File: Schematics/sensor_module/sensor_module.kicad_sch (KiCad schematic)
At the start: 4 parts, among them J1 HAL_SENS, J2 PT_1, J3 PT_2

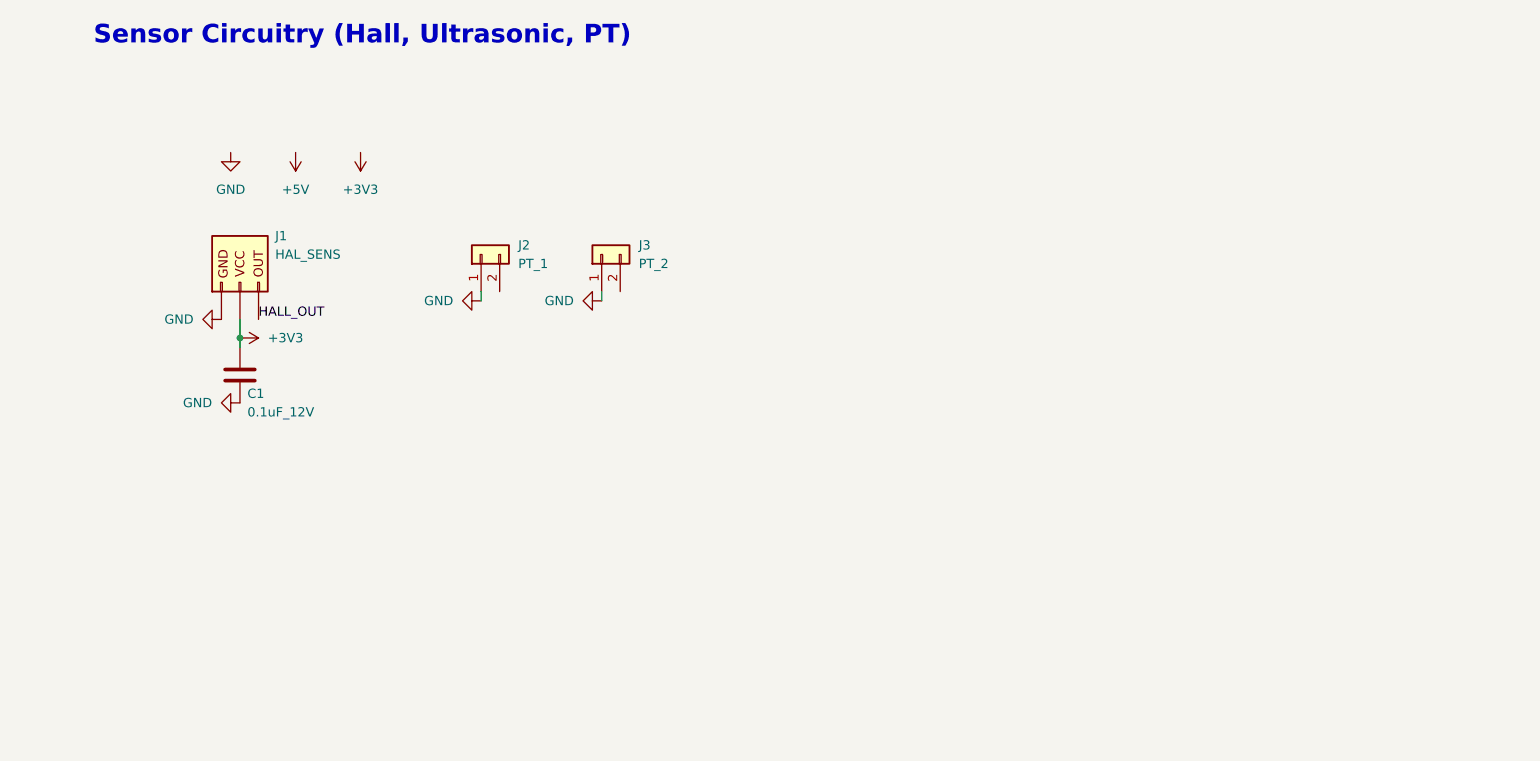
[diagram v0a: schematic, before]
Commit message: finish sensor circuitry & add sensor documentation to notion.
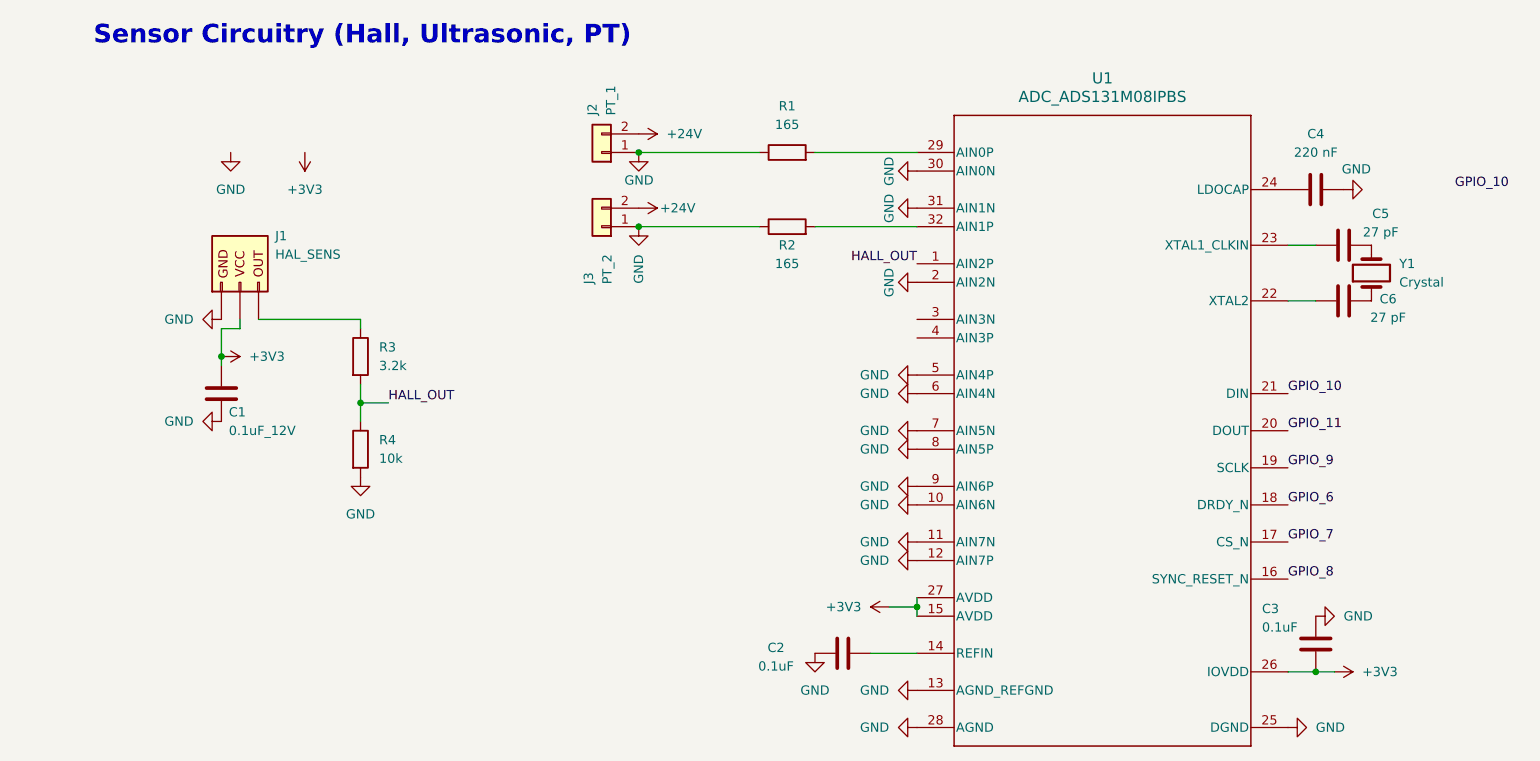
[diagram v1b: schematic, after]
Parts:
- added C2, C3: 0.1uF, symbol Device:C
- added C4: 220 nF, symbol Device:C
- added C5, C6: 27 pF, symbol Device:C
- added R1, R2: 165, symbol Device:R
- added R3: 3.2k, symbol Device:R
- added R4: 10k, symbol Device:R
- added U1: ADC_ADS131M08IPBS, PBS0032A_N, symbol 2025-11-19_23-20-52:ADS131M08IPBS
- added Y1: Crystal, symbol Device:Crystal
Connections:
- net +3V3: now also C3.2, U1.15 (AVDD), U1.26 (IOVDD), U1.27 (AVDD)
- net GND: now also C2.1, C3.1, C4.2, R1.1, R2.1, R4.2, U1.10 (AIN6N), U1.11 (AIN7N), U1.12 (AIN7P), U1.13 (AGND_REFGND), U1.2 (AIN2N), U1.25 (DGND), U1.28 (AGND), U1.30 (AIN0N), U1.31 (AIN1N), U1.5 (AIN4P), U1.6 (AIN4N), U1.7 (AIN5N), U1.8 (AIN5P), U1.9 (AIN6P)
- net HALL_OUT: now also R3.2, R4.1, U1.1 (AIN2P); no longer J1. (VCC)
- net +24V: now reaches J3.2 (Pin_2)
- net +24V: now also J2.2 (Pin_2)
- new net: R1.2, U1.29 (AIN0P)
- new net: J1. (VCC), R3.1
- new net: R2.2, U1.32 (AIN1P)
- new net: C6.1, U1.22 (XTAL2)
- new net: C6.2, Y1.1
- new net: C5.2, Y1.2
- new net: C5.1, U1.23 (XTAL1_CLKIN)
- new net: C2.2, U1.14 (REFIN)
- new net: C4.1, U1.24 (LDOCAP)
- new net GPIO_10: U1.21 (DIN)
- new net GPIO_11: U1.20 (DOUT)
- new net GPIO_6: U1.18 (DRDY_N)
- new net GPIO_7: U1.17 (CS_N)
- new net GPIO_8: U1.16 (SYNC_RESET_N)
- new net GPIO_9: U1.19 (SCLK)
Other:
- moved on the sheet: C1, J2, J3
